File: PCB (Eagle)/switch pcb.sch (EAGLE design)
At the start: 5 parts

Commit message: Update first release PCB
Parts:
- removed U$1: PINHD-1X10, adafruit:PINHD-1X10
- added U$2: PINHD-1X10, adafruit:PINHD-1X10
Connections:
- net GND: now also U$2.6; no longer U$1.6
- net INEFF+: now also U$2.1; no longer U$1.3
- net INJACK+: now also U$2.9; no longer U$1.1
- net INJACK-: now also U$2.10, U$2.2; no longer U$1.2, U$1.4
- net LED+: now also U$2.5; no longer U$1.5
- net OUTEFF+: now also U$2.3; no longer U$1.7
- net OUTJACK+: now also U$2.7; no longer U$1.9
- net OUTJACK-: now also U$2.4, U$2.8; no longer U$1.10, U$1.8
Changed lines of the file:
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@@
 <setting verticaltext="up"/>
 </settings>
-<grid distance="0.1" unitdist="inch" unit="inch" style="lines" multiple="1" display="no" altdistance="0.01" altunitdist="inch" altunit="inch"/>
+<grid distance="0.05" unitdist="inch" unit="inch" style="lines" multiple="1" display="no" altdistance="0.01" altunitdist="inch" altunit="inch"/>
 <layers>
 <layer number="1" name="Top" color="4" fill="1" visible="no" active="no"/>
@@
 <part name="R1" library="rcl" library_urn="urn:adsk.eagle:library:334" deviceset="R-EU_" device="R0603" package3d_urn="urn:adsk.eagle:package:23555/3"/>
 <part name="R2" library="rcl" library_urn="urn:adsk.eagle:library:334" deviceset="R-EU_" device="R0603" package3d_urn="urn:adsk.eagle:package:23555/3"/>
-<part name="U$1" library="adafruit" library_urn="urn:adsk.eagle:library:420" deviceset="PINHD-1X10" device="" package3d_urn="urn:adsk.eagle:package:6240656/1"/>
+<part name="U$2" library="adafruit" library_urn="urn:adsk.eagle:library:420" deviceset="PINHD-1X10" device="" package3d_urn="urn:adsk.eagle:package:6240656/1"/>
 </parts>
 <sheets>
@@
 <attribute name="VALUE" x="64.262" y="43.18" size="1.778" layer="96" rot="R90"/>
 </instance>
-<instance part="U$1" gate="G$1" x="31.75" y="91.44" smashed="yes" rot="R90">
-<attribute name="NAME" x="18.415" y="85.09" size="1.778" layer="95" rot="R90"/>
-<attribute name="VALUE" x="49.53" y="85.09" size="1.778" layer="96" rot="R90"/>
+<instance part="U$2" gate="G$1" x="31.75" y="78.74" smashed="yes" rot="R90">
+<attribute name="NAME" x="18.415" y="72.39" size="1.778" layer="95" rot="R90"/>
+<attribute name="VALUE" x="49.53" y="72.39" size="1.778" layer="96" rot="R90"/>
 </instance>
 </instances>
@@
 </net>
 <net name="INJACK+" class="0">
-<segment>
-<label x="21.59" y="60.96" size="1.778" layer="95" rot="R90"/>
-<wire x1="21.59" y1="67.31" x2="21.59" y2="88.9" width="0.1524" layer="91"/>
-<pinref part="U$1" gate="G$1" pin="1"/>
-</segment>
 <segment>
 <pinref part="S1" gate="G$1" pin="S2"/>
@@
 <junction x="48.26" y="27.94"/>
 </segment>
+<segment>
+<pinref part="U$2" gate="G$1" pin="9"/>
+<wire x1="41.91" y1="76.2" x2="41.91" y2="66.04" width="0.1524" layer="91"/>
+<label x="41.91" y="58.42" size="1.778" layer="95" rot="R90"/>
+</segment>
 </net>
 <net name="INJACK-" class="0">
 <segment>
-<wire x1="29.21" y1="88.9" x2="29.21" y2="67.31" width="0.1524" layer="91"/>
-<label x="29.21" y="60.96" size="1.778" layer="95" rot="R90"/>
-<pinref part="U$1" gate="G$1" pin="4"/>
-</segment>
-<segment>
-<wire x1="24.13" y1="88.9" x2="24.13" y2="67.31" width="0.1524" layer="91"/>
-<label x="24.13" y="60.96" size="1.778" layer="95" rot="R90"/>
-<pinref part="U$1" gate="G$1" pin="2"/>
+<pinref part="U$2" gate="G$1" pin="2"/>
+<wire x1="24.13" y1="76.2" x2="24.13" y2="66.04" width="0.1524" layer="91"/>
+<label x="24.13" y="58.42" size="1.778" layer="95" rot="R90"/>
+</segment>
+<segment>
+<pinref part="U$2" gate="G$1" pin="10"/>
+<wire x1="44.45" y1="76.2" x2="44.45" y2="66.04" width="0.1524" layer="91"/>
+<label x="44.45" y="58.42" size="1.778" layer="95" rot="R90"/>
 </segment>
 </net>
 <net name="INEFF+" class="0">
-<segment>
-<label x="26.67" y="60.96" size="1.778" layer="95" rot="R90"/>
-<wire x1="26.67" y1="67.31" x2="26.67" y2="88.9" width="0.1524" layer="91"/>
-<pinref part="U$1" gate="G$1" pin="3"/>
-</segment>
 <segment>
 <pinref part="S1" gate="G$1" pin="P2"/>
@@
 <label x="13.97" y="30.48" size="1.778" layer="95"/>
 </segment>
+<segment>
+<pinref part="U$2" gate="G$1" pin="1"/>
+<wire x1="21.59" y1="76.2" x2="21.59" y2="66.04" width="0.1524" layer="91"/>
+<label x="21.59" y="58.42" size="1.778" layer="95" rot="R90"/>
+</segment>
 </net>
 <net name="LED+" class="0">
-<segment>
-<label x="31.75" y="60.96" size="1.778" layer="95" rot="R90"/>
-<wire x1="31.75" y1="67.31" x2="31.75" y2="88.9" width="0.1524" layer="91"/>
-<pinref part="U$1" gate="G$1" pin="5"/>
-</segment>
 <segment>
 <pinref part="R2" gate="G$1" pin="2"/>
@@
 <label x="57.15" y="60.96" size="1.778" layer="95"/>
 </segment>
+<segment>
+<pinref part="U$2" gate="G$1" pin="5"/>
+<wire x1="31.75" y1="76.2" x2="31.75" y2="66.04" width="0.1524" layer="91"/>
+<label x="31.75" y="58.42" size="1.778" layer="95" rot="R90"/>
+</segment>
 </net>
 <net name="OUTEFF+" class="0">
-<segment>
-<label x="36.83" y="60.96" size="1.778" layer="95" rot="R90"/>
-<wire x1="36.83" y1="67.31" x2="36.83" y2="88.9" width="0.1524" layer="91"/>
-<pinref part="U$1" gate="G$1" pin="7"/>
-</segment>
 <segment>
 <pinref part="S1" gate="G$1" pin="S3"/>
@@
 <label x="50.8" y="17.78" size="1.778" layer="95"/>
 </segment>
+<segment>
+<pinref part="U$2" gate="G$1" pin="3"/>
+<wire x1="26.67" y1="76.2" x2="26.67" y2="66.04" width="0.1524" layer="91"/>
+<label x="26.67" y="58.42" size="1.778" layer="95" rot="R90"/>
+</segment>
 </net>
 <net name="OUTJACK-" class="0">
 <segment>
-<wire x1="44.45" y1="88.9" x2="44.45" y2="67.31" width="0.1524" layer="91"/>
-<label x="44.45" y="60.96" size="1.778" layer="95" rot="R90"/>
-<pinref part="U$1" gate="G$1" pin="10"/>
-</segment>
-<segment>
-<wire x1="39.37" y1="88.9" x2="39.37" y2="67.31" width="0.1524" layer="91"/>
-<label x="39.37" y="60.96" size="1.778" layer="95" rot="R90"/>
-<pinref part="U$1" gate="G$1" pin="8"/>
+<pinref part="U$2" gate="G$1" pin="4"/>
+<wire x1="29.21" y1="76.2" x2="29.21" y2="66.04" width="0.1524" layer="91"/>
+<label x="29.21" y="58.42" size="1.778" layer="95" rot="R90"/>
+</segment>
+<segment>
+<pinref part="U$2" gate="G$1" pin="8"/>
+<wire x1="39.37" y1="76.2" x2="39.37" y2="66.04" width="0.1524" layer="91"/>
+<label x="39.37" y="58.42" size="1.778" layer="95" rot="R90"/>
 </segment>
 </net>
 <net name="OUTJACK+" class="0">
-<segment>
-<label x="41.91" y="60.96" size="1.778" layer="95" rot="R90"/>
-<wire x1="41.91" y1="67.31" x2="41.91" y2="88.9" width="0.1524" layer="91"/>
-<pinref part="U$1" gate="G$1" pin="9"/>
-</segment>
 <segment>
 <pinref part="S1" gate="G$1" pin="P3"/>
@@
 <label x="11.43" y="20.32" size="1.778" layer="95"/>
 </segment>
+<segment>
+<pinref part="U$2" gate="G$1" pin="7"/>
+<wire x1="36.83" y1="76.2" x2="36.83" y2="66.04" width="0.1524" layer="91"/>
+<label x="36.83" y="58.42" size="1.778" layer="95" rot="R90"/>
+</segment>
 </net>
 <net name="GND" class="0">
@@
 </segment>
 <segment>
-<label x="34.29" y="60.96" size="1.778" layer="95" rot="R90"/>
-<wire x1="34.29" y1="67.31" x2="34.29" y2="88.9" width="0.1524" layer="91"/>
-<pinref part="U$1" gate="G$1" pin="6"/>
-</segment>
-</net>
+<pinref part="U$2" gate="G$1" pin="6"/>
+<wire x1="34.29" y1="76.2" x2="34.29" y2="66.04" width="0.1524" layer="91"/>
+<label x="34.29" y="58.42" size="1.778" layer="95" rot="R90"/>
+</segment>
+</net>

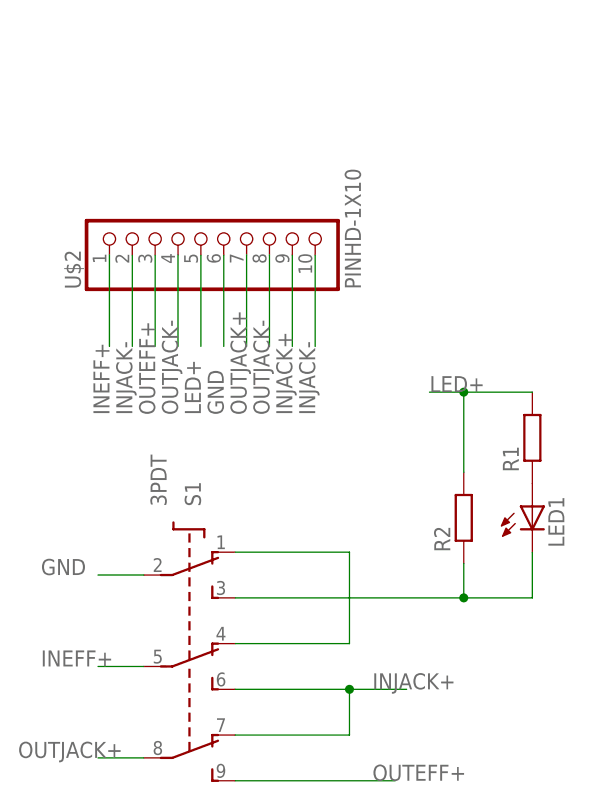
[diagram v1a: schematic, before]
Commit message: Update switchPCB to version 4423
Corrected footprint for 3PDT switch.
Updated documentation.
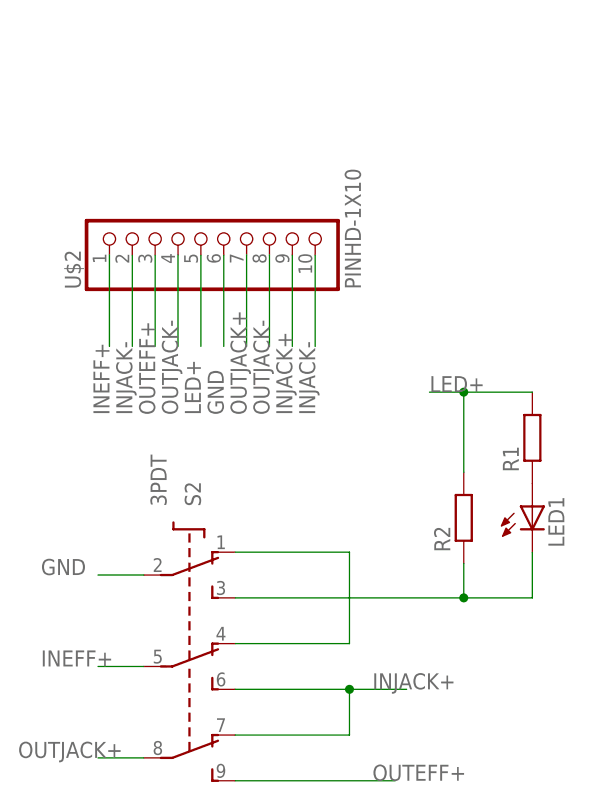
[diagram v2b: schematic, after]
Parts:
- renumbered S1 to S2
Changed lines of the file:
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@@
 </classes>
 <parts>
-<part name="S1" library="switch" library_urn="urn:adsk.eagle:library:380" deviceset="3PDT" device="" package3d_urn="urn:adsk.eagle:package:27755/1"/>
 <part name="LED1" library="adafruit" library_urn="urn:adsk.eagle:library:420" deviceset="LED" device="3MM" package3d_urn="urn:adsk.eagle:package:6240537/1"/>
 <part name="R1" library="rcl" library_urn="urn:adsk.eagle:library:334" deviceset="R-EU_" device="R0603" package3d_urn="urn:adsk.eagle:package:23555/3"/>
 <part name="R2" library="rcl" library_urn="urn:adsk.eagle:library:334" deviceset="R-EU_" device="R0603" package3d_urn="urn:adsk.eagle:package:23555/3"/>
 <part name="U$2" library="adafruit" library_urn="urn:adsk.eagle:library:420" deviceset="PINHD-1X10" device="" package3d_urn="urn:adsk.eagle:package:6240656/1"/>
+<part name="S2" library="switch" deviceset="3PDT" device="" package3d_urn="urn:adsk.eagle:package:27755/1"/>
 </parts>
 <sheets>
@@
 </plain>
 <instances>
-<instance part="S1" gate="G$1" x="30.48" y="40.64" smashed="yes" rot="R270">
-<attribute name="NAME" x="31.75" y="48.26" size="1.778" layer="95" rot="R90"/>
-<attribute name="VALUE" x="27.94" y="48.26" size="1.778" layer="96" rot="R90"/>
-</instance>
 <instance part="LED1" gate="G$1" x="68.58" y="48.26" smashed="yes">
 <attribute name="NAME" x="72.136" y="43.688" size="1.778" layer="95" rot="R90"/>
@@
 <attribute name="VALUE" x="49.53" y="72.39" size="1.778" layer="96" rot="R90"/>
 </instance>
+<instance part="S2" gate="G$1" x="30.48" y="40.64" smashed="yes" rot="R270">
+<attribute name="NAME" x="31.75" y="48.26" size="1.778" layer="95" rot="R90"/>
+<attribute name="VALUE" x="27.94" y="48.26" size="1.778" layer="96" rot="R90"/>
+</instance>
 </instances>
 <busses>
@@
 <net name="INJACK+" class="0">
 <segment>
-<pinref part="S1" gate="G$1" pin="S2"/>
 <wire x1="54.61" y1="27.94" x2="48.26" y2="27.94" width="0.1524" layer="91"/>
 <label x="50.8" y="27.94" size="1.778" layer="95"/>
-<pinref part="S1" gate="G$1" pin="O3"/>
 <wire x1="48.26" y1="27.94" x2="35.56" y2="27.94" width="0.1524" layer="91"/>
 <wire x1="35.56" y1="22.86" x2="48.26" y2="22.86" width="0.1524" layer="91"/>
 <wire x1="48.26" y1="22.86" x2="48.26" y2="27.94" width="0.1524" layer="91"/>
 <junction x="48.26" y="27.94"/>
+<pinref part="S2" gate="G$1" pin="S2"/>
+<pinref part="S2" gate="G$1" pin="O3"/>
 </segment>
 <segment>
@@
 <net name="INEFF+" class="0">
 <segment>
-<pinref part="S1" gate="G$1" pin="P2"/>
 <wire x1="25.4" y1="30.48" x2="20.32" y2="30.48" width="0.1524" layer="91"/>
 <label x="13.97" y="30.48" size="1.778" layer="95"/>
+<pinref part="S2" gate="G$1" pin="P2"/>
 </segment>
 <segment>
@@
 <net name="OUTEFF+" class="0">
 <segment>
-<pinref part="S1" gate="G$1" pin="S3"/>
 <wire x1="35.56" y1="17.78" x2="53.34" y2="17.78" width="0.1524" layer="91"/>
 <label x="50.8" y="17.78" size="1.778" layer="95"/>
+<pinref part="S2" gate="G$1" pin="S3"/>
 </segment>
 <segment>
@@
 <net name="OUTJACK+" class="0">
 <segment>
-<pinref part="S1" gate="G$1" pin="P3"/>
 <wire x1="25.4" y1="20.32" x2="20.32" y2="20.32" width="0.1524" layer="91"/>
 <label x="11.43" y="20.32" size="1.778" layer="95"/>
+<pinref part="S2" gate="G$1" pin="P3"/>
 </segment>
 <segment>
@@
 <net name="GND" class="0">
 <segment>
-<pinref part="S1" gate="G$1" pin="P1"/>
 <wire x1="25.4" y1="40.64" x2="20.32" y2="40.64" width="0.1524" layer="91"/>
 <label x="13.97" y="40.64" size="1.778" layer="95"/>
+<pinref part="S2" gate="G$1" pin="P1"/>
 </segment>
 <segment>
@@
 <net name="N$5" class="0">
 <segment>
-<pinref part="S1" gate="G$1" pin="O1"/>
 <wire x1="35.56" y1="43.18" x2="48.26" y2="43.18" width="0.1524" layer="91"/>
-<pinref part="S1" gate="G$1" pin="O2"/>
 <wire x1="48.26" y1="43.18" x2="48.26" y2="33.02" width="0.1524" layer="91"/>
 <wire x1="48.26" y1="33.02" x2="35.56" y2="33.02" width="0.1524" layer="91"/>
+<pinref part="S2" gate="G$1" pin="O1"/>
+<pinref part="S2" gate="G$1" pin="O2"/>
 </segment>
 </net>
 <net name="N$2" class="0">
 <segment>
-<pinref part="S1" gate="G$1" pin="S1"/>
 <wire x1="35.56" y1="38.1" x2="60.96" y2="38.1" width="0.1524" layer="91"/>
 <pinref part="LED1" gate="G$1" pin="C"/>
@@
 <wire x1="60.96" y1="41.91" x2="60.96" y2="38.1" width="0.1524" layer="91"/>
 <junction x="60.96" y="38.1"/>
+<pinref part="S2" gate="G$1" pin="S1"/>
 </segment>
 </net>
